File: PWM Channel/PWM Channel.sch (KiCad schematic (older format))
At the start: 2 parts, among them J101 Conn_01x05_Male

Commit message: Working on comparator
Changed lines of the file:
@@
 $Descr A4 11693 8268
 encoding utf-8
-Sheet 1 2
+Sheet 1 3
 Title ""
 Date ""
@@
 F2 "PWMCLK" O R 4500 1250 50
 $EndSheet
+$Sheet
+S 5000 1750 1250 1700
+U 61351170
+F0 "PWM" 50
+F1 "file6135116F.sch" 50
+F2 "~SELECT" I L 5000 2600 50
+F3 "CLK" I L 5000 2750 50
+F4 "COPI" I L 5000 2900 50
+F5 "DRIVER" I L 5000 2000 50
+F6 "PWMOUT" I R 6250 2550 50
+$EndSheet
+Wire Wire Line
+	4500 1250 4750 1250
+Wire Wire Line
+	4750 1250 4750 2000
+Wire Wire Line
+	4750 2000 5000 2000
 $EndSCHEMATC

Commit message: Reorganising
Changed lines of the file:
@@
 $Descr A4 11693 8268
 encoding utf-8
-Sheet 1 3
+Sheet 1 4
 Title ""
 Date ""
@@
 	1900 2400 2500 2400
 $Sheet
-S 3650 1150 850  250
+S 2850 2650 800  200
 U 613546BD
 F0 "Driver Clock" 50
 F1 "file613546BC.sch" 50
-F2 "PWMCLK" O R 4500 1250 50
+F2 "PWMCLK" O R 3650 2750 50
 $EndSheet
 $Sheet
-S 5000 1750 1250 1700
+S 3950 2700 1250 1700
 U 61351170
 F0 "PWM" 50
 F1 "file6135116F.sch" 50
-F2 "~SELECT" I L 5000 2600 50
-F3 "CLK" I L 5000 2750 50
-F4 "COPI" I L 5000 2900 50
-F5 "DRIVER" I L 5000 2000 50
-F6 "PWMOUT" I R 6250 2550 50
+F2 "DRIVER" I L 3950 2950 50
+F3 "PWMOUT" I R 5200 3500 50
+F4 "B00" I L 3950 3200 50
+F5 "B01" I L 3950 3300 50
+F6 "B02" I L 3950 3400 50
+F7 "B03" I L 3950 3500 50
+F8 "B04" I L 3950 3600 50
+F9 "B05" I L 3950 3700 50
+F10 "B06" I L 3950 3800 50
+F11 "B07" I L 3950 3900 50
+F12 "B08" I L 3950 4000 50
+F13 "B09" I L 3950 4100 50
+F14 "B10" I L 3950 4200 50
+F15 "B11" I L 3950 4300 50
+$EndSheet
+$Sheet
+S 2500 3100 800  1300
+U 613636AA
+F0 "SPI Input" 50
+F1 "file613636A9.sch" 50
+F2 "~SELECT" I L 2500 3700 50
+F3 "CLK" I L 2500 3400 50
+F4 "COPI" I L 2500 3550 50
+F5 "B00" O R 3300 3200 50
+F6 "B01" O R 3300 3300 50
+F7 "B02" O R 3300 3400 50
+F8 "B03" O R 3300 3500 50
+F9 "B04" O R 3300 3600 50
+F10 "B05" O R 3300 3700 50
+F11 "B06" O R 3300 3800 50
+F12 "B07" O R 3300 3900 50
+F13 "B08" O R 3300 4000 50
+F14 "B09" O R 3300 4100 50
+F15 "B10" O R 3300 4200 50
+F16 "B11" O R 3300 4300 50
 $EndSheet
 Wire Wire Line
-	4500 1250 4750 1250
+	3650 2750 3800 2750
 Wire Wire Line
-	4750 1250 4750 2000
+	3800 2750 3800 2950
 Wire Wire Line
-	4750 2000 5000 2000
+	3800 2950 3950 2950
+Wire Wire Line
+	3300 3200 3950 3200
+Wire Wire Line
+	3300 3300 3950 3300
+Wire Wire Line
+	3300 3400 3950 3400
+Wire Wire Line
+	3300 3500 3950 3500
+Wire Wire Line
+	3300 3600 3950 3600
+Wire Wire Line
+	3300 3700 3950 3700
+Wire Wire Line
+	3300 3800 3950 3800
+Wire Wire Line
+	3300 3900 3950 3900
+Wire Wire Line
+	3300 4000 3950 4000
+Wire Wire Line
+	3300 4100 3950 4100
+Wire Wire Line
+	3300 4200 3950 4200
+Wire Wire Line
+	3300 4300 3950 4300
 $EndSCHEMATC

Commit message: Starting rough routing
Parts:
- added D101: LED, LED_THT:LED_D5.0mm, symbol Device:LED
- added R101: R, Resistor_THT:R_Axial_DIN0207_L6.3mm_D2.5mm_P7.62mm_Horizontal, symbol Device:R
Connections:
- net GND: now also D101.1 (K)
- net PWM/PWMOUT: now also R101.2
- net SPI Input/CLK: now also J101.2 (Pin_2)
- net SPI Input/COPI: now also J101.3 (Pin_3)
- net SPI Input/~SELECT: now also J101.4 (Pin_4)
- new net: D101.2 (A), R101.1
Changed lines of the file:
@@
 Wire Wire Line
 	3300 4300 3950 4300
+$Comp
+L Device:R R101
+U 1 1 613B9292
+P 5850 3500
+F 0 "R101" V 5643 3500 50  0000 C CNN
+F 1 "R" V 5734 3500 50  0000 C CNN
+F 2 "Resistor_THT:R_Axial_DIN0207_L6.3mm_D2.5mm_P7.62mm_Horizontal" V 5780 3500 50  0001 C CNN
+F 3 "~" H 5850 3500 50  0001 C CNN
+	1    5850 3500
+	0    1    1    0
+$EndComp
+$Comp
+L Device:LED D101
+U 1 1 613BA23C
+P 6550 3500
+F 0 "D101" H 6543 3245 50  0000 C CNN
+F 1 "LED" H 6543 3336 50  0000 C CNN
+F 2 "LED_THT:LED_D5.0mm" H 6550 3500 50  0001 C CNN
+F 3 "~" H 6550 3500 50  0001 C CNN
+	1    6550 3500
+	-1   0    0    1
+$EndComp
+$Comp
+L power:GND #PWR0113
+U 1 1 613BAA40
+P 7050 3700
+F 0 "#PWR0113" H 7050 3450 50  0001 C CNN
+F 1 "GND" H 7055 3527 50  0000 C CNN
+F 2 "" H 7050 3700 50  0001 C CNN
+F 3 "" H 7050 3700 50  0001 C CNN
+	1    7050 3700
+	1    0    0    -1
+$EndComp
+Wire Wire Line
+	5200 3500 5700 3500
+Wire Wire Line
+	6000 3500 6400 3500
+Wire Wire Line
+	6700 3500 7050 3500
+Wire Wire Line
+	7050 3500 7050 3700
+Wire Wire Line
+	1400 2100 1650 2100
+Wire Wire Line
+	1650 2100 1650 3400
+Wire Wire Line
+	1650 3400 2500 3400
+Wire Wire Line
+	1400 2200 1600 2200
+Wire Wire Line
+	1600 2200 1600 3550
+Wire Wire Line
+	1600 3550 2500 3550
+Wire Wire Line
+	1400 2300 1550 2300
+Wire Wire Line
+	1550 2300 1550 3700
+Wire Wire Line
+	1550 3700 2500 3700
 $EndSCHEMATC

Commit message: Preliminary routing
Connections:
- net SPI Input/CLK: now also J101.4 (Pin_4); no longer J101.2 (Pin_2)
- net SPI Input/~SELECT: now also J101.2 (Pin_2); no longer J101.4 (Pin_4)
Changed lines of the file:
@@
 	1400 2100 1650 2100
-Wire Wire Line
-	1650 2100 1650 3400
-Wire Wire Line
-	1650 3400 2500 3400
 Wire Wire Line
 	1400 2200 1600 2200
@@
 	1400 2300 1550 2300
 Wire Wire Line
-	1550 2300 1550 3700
+	1650 3700 2500 3700
 Wire Wire Line
-	1550 3700 2500 3700
+	1650 2100 1650 3700
+Wire Wire Line
+	2500 3400 1550 3400
+Wire Wire Line
+	1550 3400 1550 2300
 $EndSCHEMATC

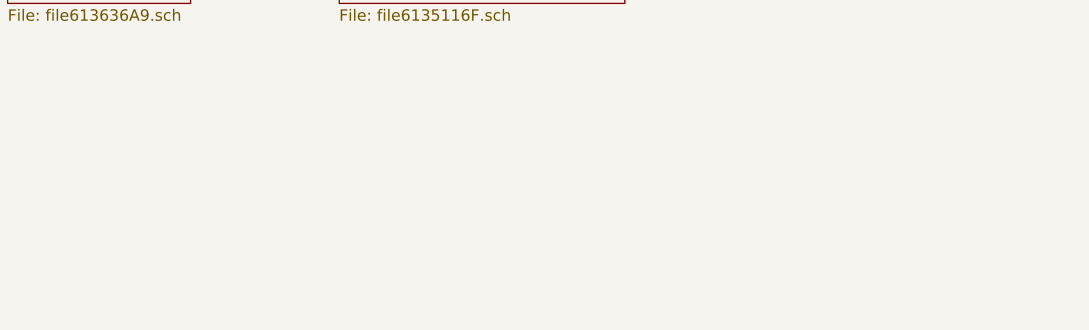
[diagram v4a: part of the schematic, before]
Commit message: Add mounting holes
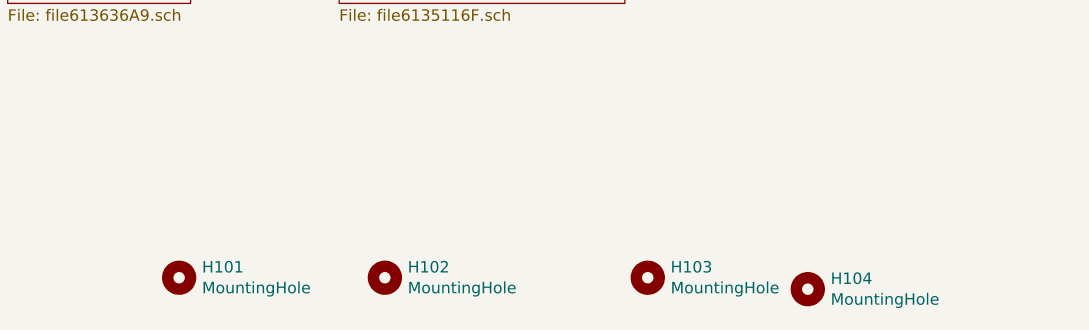
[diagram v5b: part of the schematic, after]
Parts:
- added H101, H102, H103, H104: MountingHole, MountingHole:MountingHole_2.7mm_M2.5, symbol Mechanical:MountingHole
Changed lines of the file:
@@
 Wire Wire Line
 	1550 3400 1550 2300
+$Comp
+L Mechanical:MountingHole H101
+U 1 1 6136B6F5
+P 3250 5600
+F 0 "H101" H 3350 5646 50  0000 L CNN
+F 1 "MountingHole" H 3350 5555 50  0000 L CNN
+F 2 "MountingHole:MountingHole_2.7mm_M2.5" H 3250 5600 50  0001 C CNN
+F 3 "~" H 3250 5600 50  0001 C CNN
+	1    3250 5600
+	1    0    0    -1
+$EndComp
+$Comp
+L Mechanical:MountingHole H102
+U 1 1 6136BC38
+P 4150 5600
+F 0 "H102" H 4250 5646 50  0000 L CNN
+F 1 "MountingHole" H 4250 5555 50  0000 L CNN
+F 2 "MountingHole:MountingHole_2.7mm_M2.5" H 4150 5600 50  0001 C CNN
+F 3 "~" H 4150 5600 50  0001 C CNN
+	1    4150 5600
+	1    0    0    -1
+$EndComp
+$Comp
+L Mechanical:MountingHole H103
+U 1 1 6136C4A2
+P 5300 5600
+F 0 "H103" H 5400 5646 50  0000 L CNN
+F 1 "MountingHole" H 5400 5555 50  0000 L CNN
+F 2 "MountingHole:MountingHole_2.7mm_M2.5" H 5300 5600 50  0001 C CNN
+F 3 "~" H 5300 5600 50  0001 C CNN
+	1    5300 5600
+	1    0    0    -1
+$EndComp
+$Comp
+L Mechanical:MountingHole H104
+U 1 1 6136CB85
+P 6000 5650
+F 0 "H104" H 6100 5696 50  0000 L CNN
+F 1 "MountingHole" H 6100 5605 50  0000 L CNN
+F 2 "MountingHole:MountingHole_2.7mm_M2.5" H 6000 5650 50  0001 C CNN
+F 3 "~" H 6000 5650 50  0001 C CNN
+	1    6000 5650
+	1    0    0    -1
+$EndComp
 $EndSCHEMATC

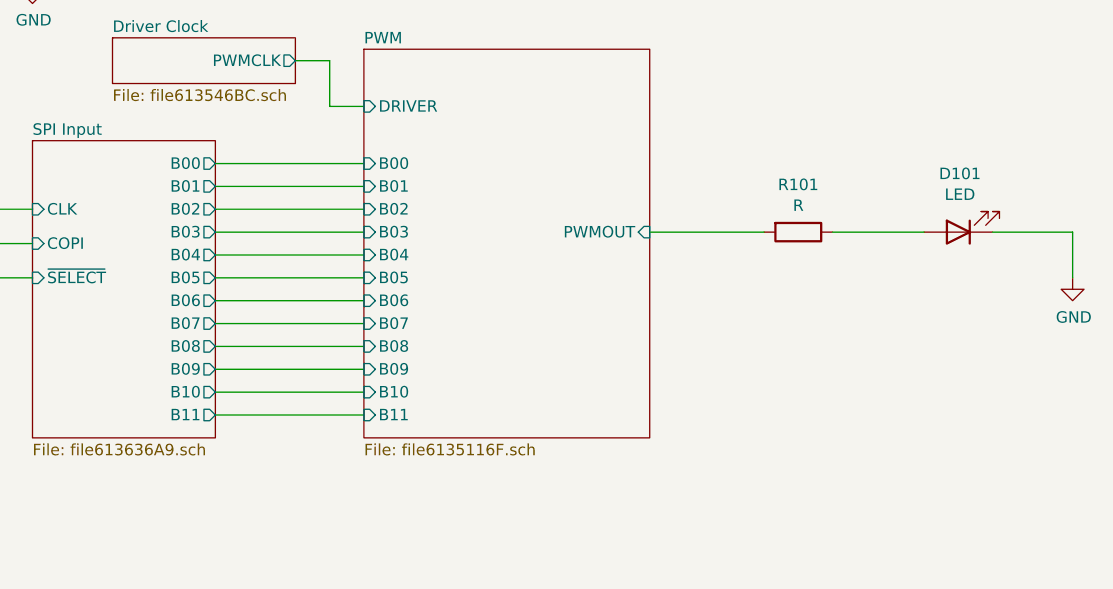
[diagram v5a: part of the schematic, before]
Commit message: Updates to PWM Channel Board (#6)
Add a number of LED indicators and reduce from 12-bit to 8-bit
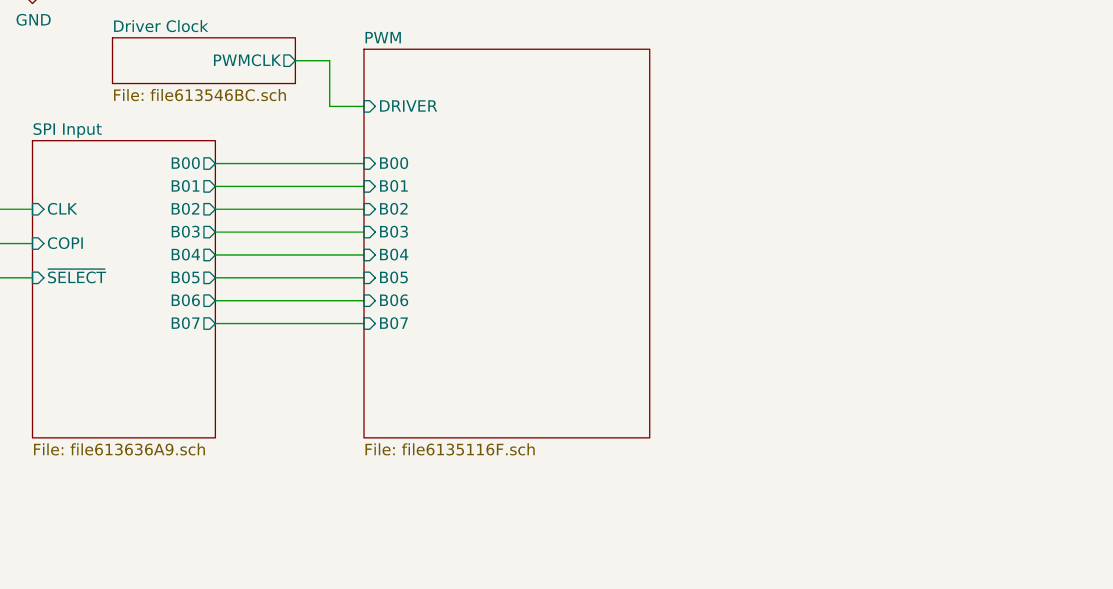
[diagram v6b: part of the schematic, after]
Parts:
- removed D101: LED, LED_THT:LED_D5.0mm, symbol Device:LED
- removed R101: R, Resistor_THT:R_Axial_DIN0207_L6.3mm_D2.5mm_P7.62mm_Horizontal, symbol Device:R
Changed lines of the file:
@@
 F1 "file6135116F.sch" 50
 F2 "DRIVER" I L 3950 2950 50
-F3 "PWMOUT" I R 5200 3500 50
-F4 "B00" I L 3950 3200 50
-F5 "B01" I L 3950 3300 50
-F6 "B02" I L 3950 3400 50
-F7 "B03" I L 3950 3500 50
-F8 "B04" I L 3950 3600 50
-F9 "B05" I L 3950 3700 50
-F10 "B06" I L 3950 3800 50
-F11 "B07" I L 3950 3900 50
-F12 "B08" I L 3950 4000 50
-F13 "B09" I L 3950 4100 50
-F14 "B10" I L 3950 4200 50
-F15 "B11" I L 3950 4300 50
+F3 "B00" I L 3950 3200 50
+F4 "B01" I L 3950 3300 50
+F5 "B02" I L 3950 3400 50
+F6 "B03" I L 3950 3500 50
+F7 "B04" I L 3950 3600 50
+F8 "B05" I L 3950 3700 50
+F9 "B06" I L 3950 3800 50
+F10 "B07" I L 3950 3900 50
 $EndSheet
 $Sheet
@@
 F11 "B06" O R 3300 3800 50
 F12 "B07" O R 3300 3900 50
-F13 "B08" O R 3300 4000 50
-F14 "B09" O R 3300 4100 50
-F15 "B10" O R 3300 4200 50
-F16 "B11" O R 3300 4300 50
 $EndSheet
 Wire Wire Line
@@
 	3300 3900 3950 3900
 Wire Wire Line
-	3300 4000 3950 4000
-Wire Wire Line
-	3300 4100 3950 4100
-Wire Wire Line
-	3300 4200 3950 4200
-Wire Wire Line
-	3300 4300 3950 4300
-$Comp
-L Device:R R101
-U 1 1 613B9292
-P 5850 3500
-F 0 "R101" V 5643 3500 50  0000 C CNN
-F 1 "R" V 5734 3500 50  0000 C CNN
-F 2 "Resistor_THT:R_Axial_DIN0207_L6.3mm_D2.5mm_P7.62mm_Horizontal" V 5780 3500 50  0001 C CNN
-F 3 "~" H 5850 3500 50  0001 C CNN
-	1    5850 3500
-	0    1    1    0
-$EndComp
-$Comp
-L Device:LED D101
-U 1 1 613BA23C
-P 6550 3500
-F 0 "D101" H 6543 3245 50  0000 C CNN
-F 1 "LED" H 6543 3336 50  0000 C CNN
-F 2 "LED_THT:LED_D5.0mm" H 6550 3500 50  0001 C CNN
-F 3 "~" H 6550 3500 50  0001 C CNN
-	1    6550 3500
-	-1   0    0    1
-$EndComp
-$Comp
-L power:GND #PWR0113
-U 1 1 613BAA40
-P 7050 3700
-F 0 "#PWR0113" H 7050 3450 50  0001 C CNN
-F 1 "GND" H 7055 3527 50  0000 C CNN
-F 2 "" H 7050 3700 50  0001 C CNN
-F 3 "" H 7050 3700 50  0001 C CNN
-	1    7050 3700
-	1    0    0    -1
-$EndComp
-Wire Wire Line
-	5200 3500 5700 3500
-Wire Wire Line
-	6000 3500 6400 3500
-Wire Wire Line
-	6700 3500 7050 3500
-Wire Wire Line
-	7050 3500 7050 3700
-Wire Wire Line
 	1400 2100 1650 2100
 Wire Wire Line
-	1400 2200 1600 2200
-Wire Wire Line
 	1600 2200 1600 3550
-Wire Wire Line
-	1600 3550 2500 3550
 Wire Wire Line
 	1400 2300 1550 2300
@@
 	1    0    0    -1
 $EndComp
+Wire Wire Line
+	1400 2200 1600 2200
+Wire Wire Line
+	1600 3550 2500 3550
 $EndSCHEMATC
